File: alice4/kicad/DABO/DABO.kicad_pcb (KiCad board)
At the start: 2 copper layers, 41.5 x 97.9 mm, 8 parts, among them P3 CONN_02X20, P4 CONN_02X07, U1 touchscreen_controller, U2 LCDBREAKOUT

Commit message: DISPLAY_ENABLE -> DATA_ENABLE
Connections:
- net DISPLAY_ENABLE renamed DATA_ENABLE
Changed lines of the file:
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@@
   (net 19 X-)
   (net 20 Y+)
-  (net 21 DISPLAY_ENABLE)
+  (net 21 DATA_ENABLE)
   (net 22 VSYNC)
   (net 23 HSYNC)
@@
     (add_net B7)
     (add_net BACKLIGHT_PWM)
-    (add_net DISPLAY_ENABLE)
+    (add_net DATA_ENABLE)
     (add_net DISPLAY_ON)
     (add_net G0)
@@
       (net 17 X+))
     (pad 21 thru_hole oval (at 24.13 -11.43 270) (size 1.2 2) (drill 0.8) (layers *.Cu *.Mask F.SilkS)
-      (net 21 DISPLAY_ENABLE))
+      (net 21 DATA_ENABLE))
     (pad 20 thru_hole oval (at 24.13 11.43 270) (size 1.2 2) (drill 0.8) (layers *.Cu *.Mask F.SilkS)
       (net 20 Y+))
@@
       (net 13 B4))
     (pad 28 thru_hole oval (at 2.54 33.02) (size 1.7272 1.7272) (drill 1.016) (layers *.Cu *.Mask F.SilkS)
-      (net 21 DISPLAY_ENABLE))
+      (net 21 DATA_ENABLE))
     (pad 29 thru_hole oval (at 0 35.56) (size 1.7272 1.7272) (drill 1.016) (layers *.Cu *.Mask F.SilkS)
       (net 36 "Net-(P3-Pad29)"))

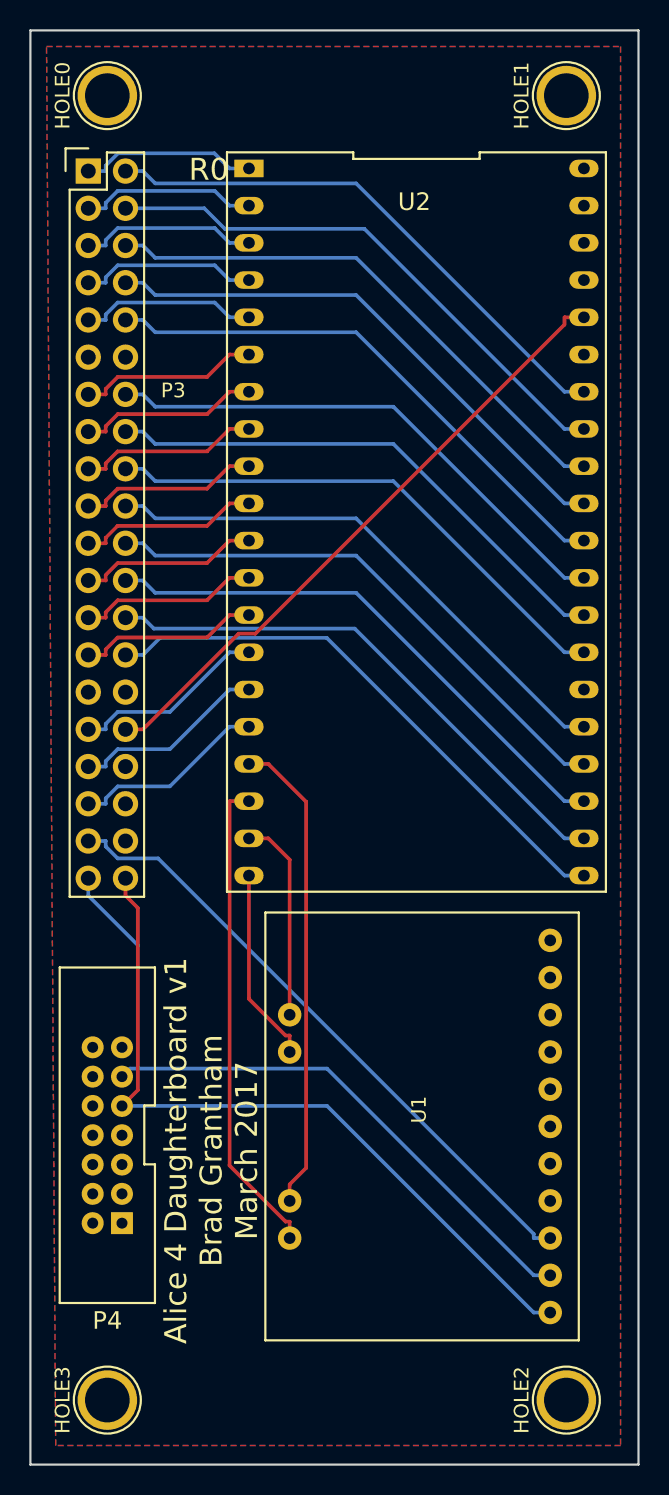
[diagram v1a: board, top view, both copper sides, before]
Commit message: Spin DABO 1.5 for PCBWay
Add pullups

Drop 14-pin connector

Fix 3v3 to the STMPE811 breakout
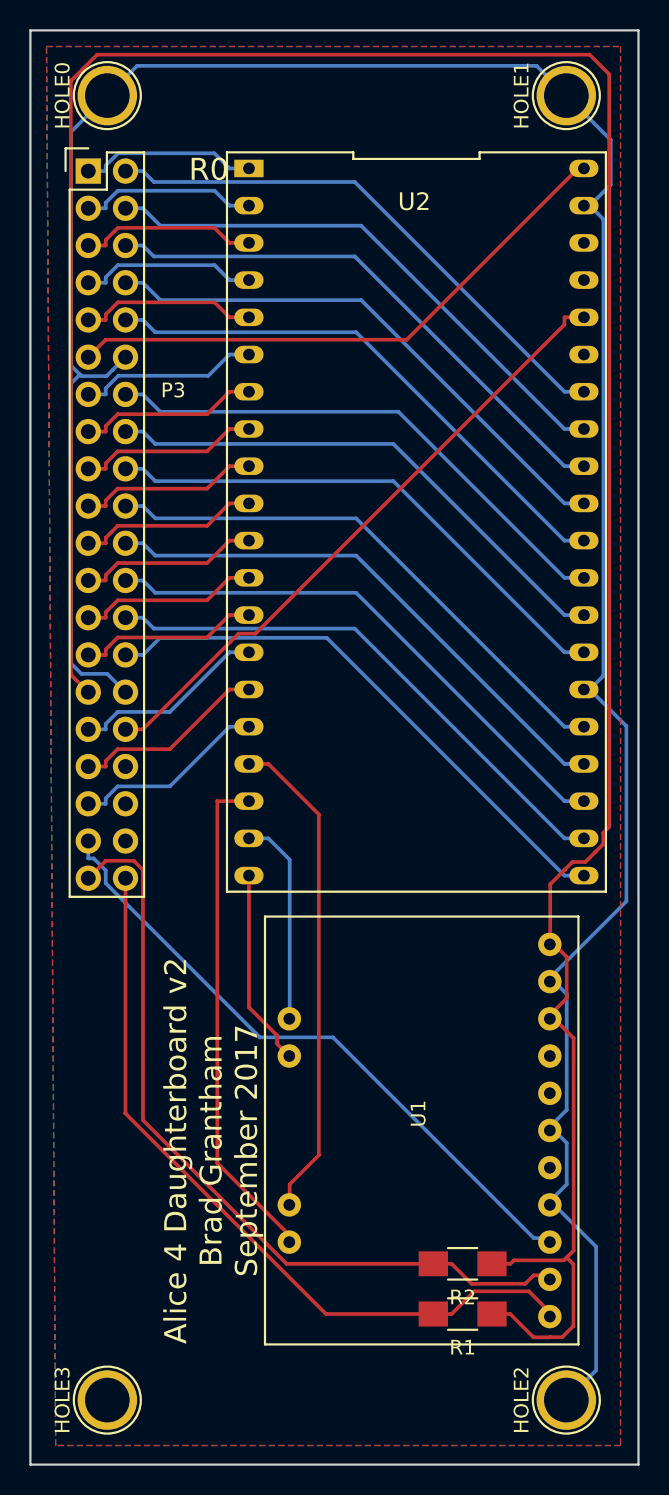
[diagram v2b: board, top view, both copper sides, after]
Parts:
- removed P4: CONN_02X07, DIH_2x7x2mm:DIH_2x7x2mm
- added R1: 3.3, Resistors_SMD:R_1206_HandSoldering, F.Cu at (161.2, 136.4)
- added R2: 3.3, Resistors_SMD:R_1206_HandSoldering, F.Cu at (161.2, 133.0)
- moved U1 0.28 mm to (149.4, 108.6)
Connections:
- P3 pad 29: Net-(P3-Pad29) -> +3V3
- U1 pad 13: Net-(U1-Pad13) -> +3V3
- U1 pad 15: +5V -> +3V3
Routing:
- net +3V3: track 0.00 -> 181.6 mm
- net GND: track 0.00 -> 181.2 mm
- net +5V: track 0.00 -> 39.2 mm
- net SCL: track 49.7 -> 54.2 mm
- net Y-: track 33.0 -> 34.0 mm
- net INT: track 43.1 -> 44.0 mm
- net X-: track 32.7 -> 33.4 mm
- net SDA: track 51.4 -> 52.0 mm
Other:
- board text added: "Alice 4 Daughterboard v2 Brad Grantham September 2017"
- board text removed: "Alice 4 Daughterboard v1 Brad Grantham March 2017"
